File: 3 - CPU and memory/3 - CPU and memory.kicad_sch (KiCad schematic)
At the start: 48 parts, among them J1 EDGE, U1 74AC00, U10 74HC563, U2 74AC32, U3 74AC138, U4 Z84C0010, U5 SST39SF010, U6 AS6C4008, U7 74AC32, U8 74AC174, U9 74HC563

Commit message: Finished cleaning up the project
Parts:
- U10, U9: symbol 0 - Library:74HC563 -> 0_Library:74HC563
- U4: symbol 0 - Library:Z84C00xx CPU -> 0_Library:Z84C00xx CPU
- U5: symbol 0 - Library:SST39SF010 -> 0_Library:SST39SF010
- U6: symbol 0 - Library:AS6C4008 -> 0_Library:AS6C4008
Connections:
- net +5V: now also J1.2 (A2), J1.30 (A30), J1.33 (B2), J1.61 (B30)
- net A0: now also J1.18 (A18)
- net A1: now also J1.17 (A17)
- net A10: now also J1.8 (A8)
- net A11: now also J1.7 (A7)
- net A12: now also J1.6 (A6)
- net A13: now also J1.5 (A5)
- net A14: now also J1.4 (A4)
- net A15: now also J1.3 (A3)
- net A2: now also J1.16 (A16)
- net A3: now also J1.15 (A15)
- net A4: now also J1.14 (A14)
- net A5: now also J1.13 (A13)
- net A6: now also J1.12 (A12)
- net A7: now also J1.11 (A11)
- net A8: now also J1.10 (A10)
- net A9: now also J1.9 (A9)
- net CLK: now also J1.36 (B5)
- net D0: now also J1.19 (A19)
- net D1: now also J1.20 (A20)
- net D2: now also J1.21 (A21)
- net D3: now also J1.22 (A22)
- net D4: now also J1.23 (A23)
- net D5: now also J1.24 (A24)
- net D6: now also J1.25 (A25)
- net D7: now also J1.26 (A26)
- net GND: now also J1.1 (A1), J1.31 (A31), J1.32 (B1), J1.62 (B31)
- net ~{BUSAK}: now also J1.44 (B13)
- net ~{BUSRQ}: now also J1.46 (B15)
- net ~{CLK_SEL}: now also J1.50 (B19)
- net ~{CLK}: now also J1.60 (B29)
- net ~{HALT}: now also J1.45 (B14)
- net ~{INT}: now also J1.37 (B6)
- net ~{IORQ}: now also J1.41 (B10)
- net ~{M1}: now also J1.34 (B3)
- net ~{MREQ}: now also J1.38 (B7)
- net ~{NMI}: now also J1.48 (B17)
- net ~{RD}: now also J1.40 (B9)
- net ~{RESET}: now also J1.35 (B4)
- net ~{WAIT}: now also J1.47 (B16)
- net ~{WR}: now also J1.39 (B8)
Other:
- moved on the sheet: J1

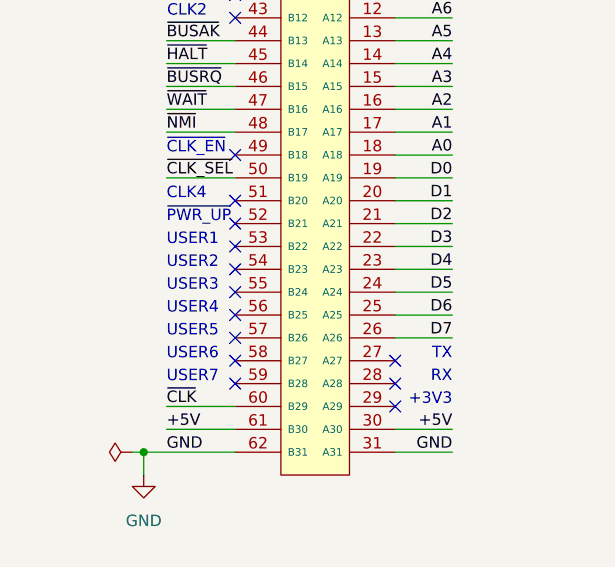
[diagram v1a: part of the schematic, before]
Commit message: Added serial card, still needs work
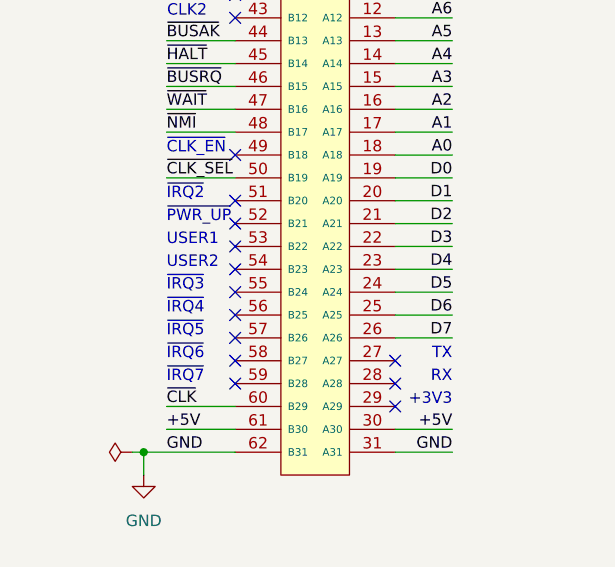
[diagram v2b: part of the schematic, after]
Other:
- note added: "~{IRQ2}"
- note added: "~{IRQ3}"
- note added: "~{IRQ4}"
- note added: "~{IRQ5}"
- note added: "~{IRQ6}"
- note added: "~{IRQ7}"
- note removed: "CLK4"
- note removed: "USER3"
- note removed: "USER4"
- note removed: "USER5"
- note removed: "USER6"
- note removed: "USER7"
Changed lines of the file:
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@@
     (effects (font (size 1.27 1.27)) (justify right bottom))
+  )
+  (text "~{IRQ7}" (at 31.75 107.95 0)
+    (effects (font (size 1.27 1.27)) (justify left bottom))
   )
   (text "00h-07h (SIO_CS)" (at 158.75 39.37 0)
@@
     (effects (font (size 2.54 2.54) (thickness 0.508) bold) (justify left bottom))
   )
+  (text "~{IRQ3}" (at 31.75 97.79 0)
+    (effects (font (size 1.27 1.27)) (justify left bottom))
+  )
   (text "BUS" (at 31.75 27.94 0)
     (effects (font (size 2.54 2.54) (thickness 0.508) bold) (justify left bottom))
@@
     (effects (font (size 1.27 1.27)) (justify left bottom))
   )
+  (text "~{IRQ5}" (at 31.75 102.87 0)
+    (effects (font (size 1.27 1.27)) (justify left bottom))
+  )
   (text "CPU & MEMORY" (at 204.47 80.01 0)
     (effects (font (size 2.54 2.54) (thickness 0.508) bold) (justify left bottom))
+  )
+  (text "~{IRQ2}" (at 31.75 87.63 0)
+    (effects (font (size 1.27 1.27)) (justify left bottom))
   )
   (text "CLK2" (at 31.8014 67.3536 0)
     (effects (font (size 1.27 1.27)) (justify left bottom))
   )
-  (text "CLK4" (at 31.75 87.63 0)
+  (text "~{IRQ6}" (at 31.75 105.41 0)
+    (effects (font (size 1.27 1.27)) (justify left bottom))
+  )
+  (text "~{IRQ4}" (at 31.75 100.33 0)
     (effects (font (size 1.27 1.27)) (justify left bottom))
   )
   (text "+3V3" (at 63.5 110.49 0)
     (effects (font (size 1.27 1.27)) (justify right bottom))
-  )
-  (text "USER5" (at 31.75 102.8898 0)
-    (effects (font (size 1.27 1.27)) (justify left bottom))
-  )
-  (text "USER3" (at 31.75 97.8098 0)
-    (effects (font (size 1.27 1.27)) (justify left bottom))
   )
   (text "USER2" (at 31.75 95.2698 0)
@@
   )
   (text "10h-17h (KEY_WR)" (at 158.75 44.45 0)
-    (effects (font (size 1.27 1.27)) (justify left bottom))
-  )
-  (text "USER4" (at 31.75 100.3498 0)
     (effects (font (size 1.27 1.27)) (justify left bottom))
   )
@@
     (effects (font (size 1.27 1.27)) (justify right bottom))
   )
-  (text "USER6" (at 31.75 105.4298 0)
-    (effects (font (size 1.27 1.27)) (justify left bottom))
-  )
   (text "~{MR}" (at 31.75 64.77 0)
     (effects (font (size 1.27 1.27)) (justify left bottom))
   )
-  (text "USER7" (at 31.75 107.9698 0)
-    (effects (font (size 1.27 1.27)) (justify left bottom))
-  )

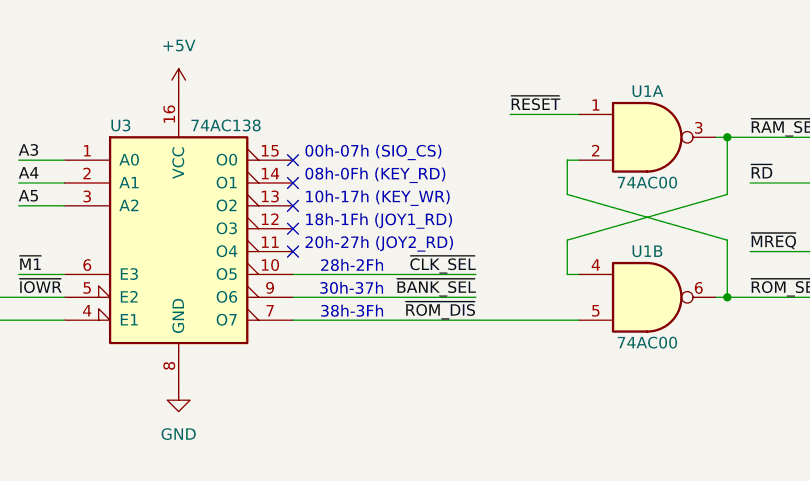
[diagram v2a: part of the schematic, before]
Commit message: Made a mess of things a bit.
Software clock is non-functional. Worked on the breadboard, but makes the CPU board crash when writing to the IO port to select clock speed.
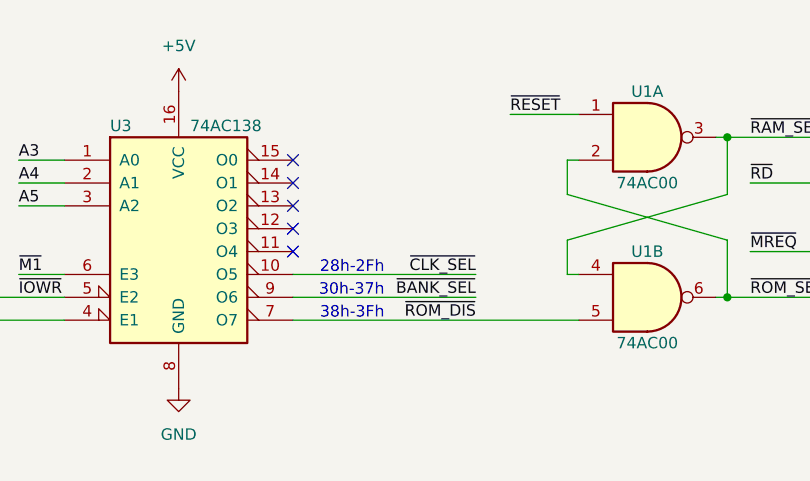
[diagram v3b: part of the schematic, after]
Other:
- note removed: "00h-07h (SIO_CS)"
- note removed: "08h-0Fh (KEY_RD)"
- note removed: "10h-17h (KEY_WR)"
- note removed: "18h-1Fh (JOY1_RD)"
- note removed: "20h-27h (JOY2_RD)"
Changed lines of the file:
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@@
     (stroke (width 0) (type default))
-  )
-  (text "08h-0Fh (KEY_RD)" (at 158.75 41.91 0)
-    (effects (font (size 1.27 1.27)) (justify left bottom))
   )
   (text "~{CLK_EN}" (at 31.75 82.55 0)
@@
     (effects (font (size 1.27 1.27)) (justify left bottom))
   )
-  (text "00h-07h (SIO_CS)" (at 158.75 39.37 0)
-    (effects (font (size 1.27 1.27)) (justify left bottom))
-  )
   (text "BLINKENLIGHTS" (at 101.6 167.64 0)
     (effects (font (size 2.54 2.54) (thickness 0.508) bold) (justify left bottom))
@@
   (text "BUS" (at 31.75 27.94 0)
     (effects (font (size 2.54 2.54) (thickness 0.508) bold) (justify left bottom))
-  )
-  (text "18h-1Fh (JOY1_RD)" (at 158.75 46.99 0)
-    (effects (font (size 1.27 1.27)) (justify left bottom))
   )
   (text "~{IRQ5}" (at 31.75 102.87 0)
@@
     (effects (font (size 1.27 1.27)) (justify right bottom))
   )
-  (text "10h-17h (KEY_WR)" (at 158.75 44.45 0)
-    (effects (font (size 1.27 1.27)) (justify left bottom))
-  )
-  (text "20h-27h (JOY2_RD)" (at 158.75 49.53 0)
-    (effects (font (size 1.27 1.27)) (justify left bottom))
-  )
   (text "BANK SWITCHING" (at 102.87 80.01 0)
